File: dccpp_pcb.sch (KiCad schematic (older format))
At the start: 9 parts

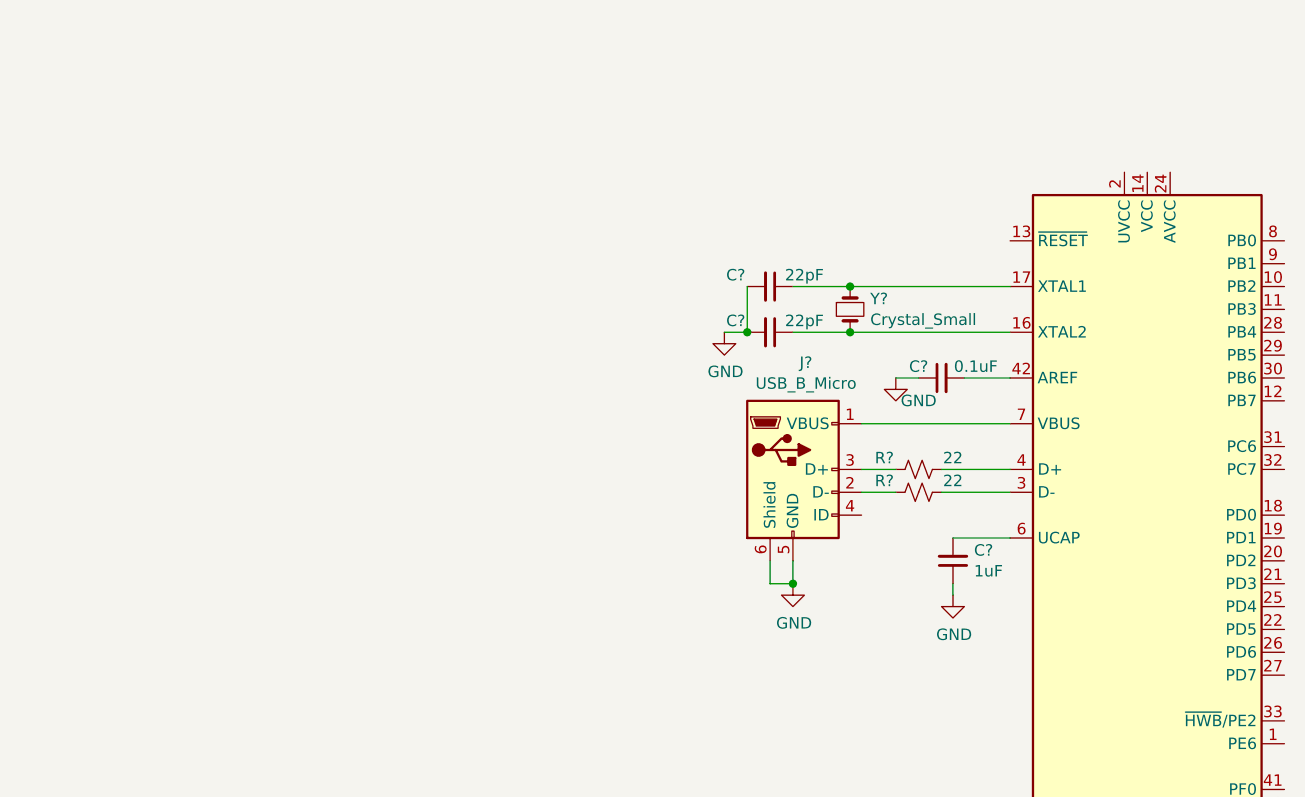
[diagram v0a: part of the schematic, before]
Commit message: Add datasheets and 5V
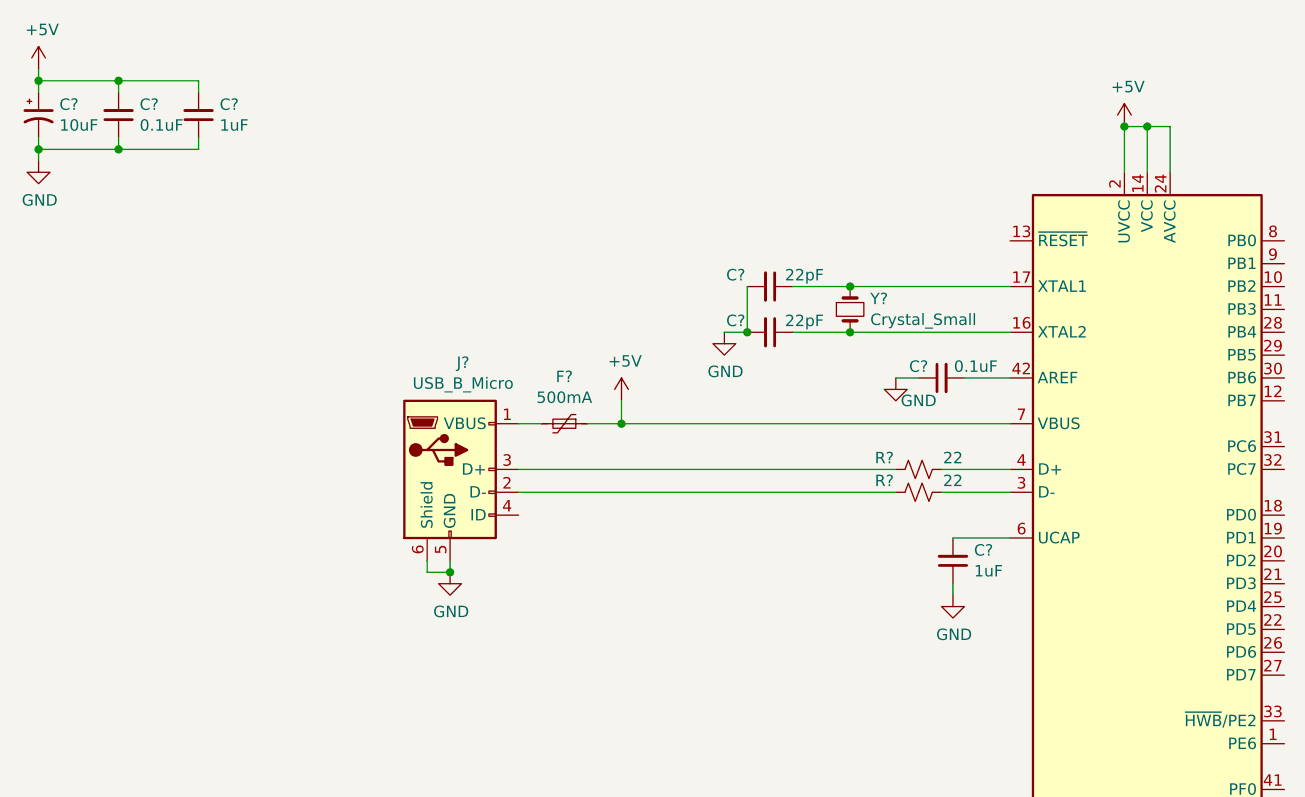
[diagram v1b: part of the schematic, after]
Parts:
- added C?: 1uF, symbol Device:C_Small
- added C?: 0.1uF, symbol Device:C_Small
- added C?: 10uF, symbol Device:CP1_Small
- added F?: 500mA, symbol Device:Polyfuse_Small
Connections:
- net GND: now also C?.1, C?.1, C?.2
- net +5V: now reaches U?.14 (VCC), U?.34 (VCC)
- net +5V: now also U?.2 (UVCC), U?.24 (AVCC), U?.44 (AVCC), U?.7 (VBUS), C?.1, C?.2, C?.2, F?.1
- net at J?.1 (VBUS): now also F?.2; no longer U?.7 (VBUS)
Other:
- moved on the sheet: J?
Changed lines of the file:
@@
 L Connector:USB_B_Micro J?
 U 1 1 5CDAE7D1
-P 4000 2500
-F 0 "J?" H 4057 2967 50  0000 C CNN
-F 1 "USB_B_Micro" H 4057 2876 50  0000 C CNN
-F 2 "" H 4150 2450 50  0001 C CNN
-F 3 "~" H 4150 2450 50  0001 C CNN
-	1    4000 2500
+P 2500 2500
+F 0 "J?" H 2557 2967 50  0000 C CNN
+F 1 "USB_B_Micro" H 2557 2876 50  0000 C CNN
+F 2 "" H 2650 2450 50  0001 C CNN
+F 3 "~" H 2650 2450 50  0001 C CNN
+	1    2500 2500
 	1    0    0    -1
 $EndComp
 Wire Wire Line
 	4450 2100 4550 2100
-Wire Wire Line
-	4300 2300 4950 2300
 $Comp
 L power:GND #PWR?
 U 1 1 5CDB18D1
-P 4000 3000
-F 0 "#PWR?" H 4000 2750 50  0001 C CNN
-F 1 "GND" H 4005 2827 50  0000 C CNN
-F 2 "" H 4000 3000 50  0001 C CNN
-F 3 "" H 4000 3000 50  0001 C CNN
-	1    4000 3000
+P 2500 2950
+F 0 "#PWR?" H 2500 2700 50  0001 C CNN
+F 1 "GND" H 2505 2777 50  0000 C CNN
+F 2 "" H 2500 2950 50  0001 C CNN
+F 3 "" H 2500 2950 50  0001 C CNN
+	1    2500 2950
 	1    0    0    -1
 $EndComp
 Wire Wire Line
-	4000 3000 4000 2900
+	2500 2950 2500 2900
 Wire Wire Line
-	3900 2900 3900 3000
+	2400 2900 2400 2950
 Wire Wire Line
-	3900 3000 4000 3000
-Connection ~ 4000 3000
+	2400 2950 2500 2950
+Connection ~ 2500 2950
 $Comp
 L Device:R_Small_US R?
@@
 $EndComp
 Wire Wire Line
-	4300 2500 4450 2500
+	2800 2500 4450 2500
 Wire Wire Line
-	4450 2600 4300 2600
+	4450 2600 2800 2600
 Wire Wire Line
 	4650 2600 4950 2600
 Wire Wire Line
 	4950 2500 4650 2500
+$Comp
+L Device:Polyfuse_Small F?
+U 1 1 5CDC3346
+P 3000 2300
+F 0 "F?" V 2795 2300 50  0000 C CNN
+F 1 "500mA" V 2886 2300 50  0000 C CNN
+F 2 "" H 3050 2100 50  0001 L CNN
+F 3 "~" H 3000 2300 50  0001 C CNN
+	1    3000 2300
+	0    1    1    0
+$EndComp
+Wire Wire Line
+	2800 2300 2900 2300
+$Comp
+L power:+5V #PWR?
+U 1 1 5CDC41B4
+P 3250 2200
+F 0 "#PWR?" H 3250 2050 50  0001 C CNN
+F 1 "+5V" H 3265 2373 50  0000 C CNN
+F 2 "" H 3250 2200 50  0001 C CNN
+F 3 "" H 3250 2200 50  0001 C CNN
+	1    3250 2200
+	1    0    0    -1
+$EndComp
+$Comp
+L power:+5V #PWR?
+U 1 1 5CDC4BA0
+P 5450 1000
+F 0 "#PWR?" H 5450 850 50  0001 C CNN
+F 1 "+5V" H 5465 1173 50  0000 C CNN
+F 2 "" H 5450 1000 50  0001 C CNN
+F 3 "" H 5450 1000 50  0001 C CNN
+	1    5450 1000
+	1    0    0    -1
+$EndComp
+Wire Wire Line
+	3100 2300 3250 2300
+Wire Wire Line
+	5450 1000 5550 1000
+Wire Wire Line
+	5650 1000 5650 1200
+Wire Wire Line
+	5550 1200 5550 1000
+Connection ~ 5550 1000
+Wire Wire Line
+	5550 1000 5650 1000
+Wire Wire Line
+	5450 1200 5450 1000
+Connection ~ 5450 1000
+$Comp
+L Device:C_Small C?
+U 1 1 5CDC7BF0
+P 1400 950
+F 0 "C?" H 1308 904 50  0000 R CNN
+F 1 "1uF" H 1308 995 50  0000 R CNN
+F 2 "" H 1400 950 50  0001 C CNN
+F 3 "~" H 1400 950 50  0001 C CNN
+	1    1400 950
+	-1   0    0    1
+$EndComp
+$Comp
+L Device:C_Small C?
+U 1 1 5CDCB75C
+P 1050 950
+F 0 "C?" H 958 904 50  0000 R CNN
+F 1 "0.1uF" H 958 995 50  0000 R CNN
+F 2 "" H 1050 950 50  0001 C CNN
+F 3 "~" H 1050 950 50  0001 C CNN
+	1    1050 950
+	-1   0    0    1
+$EndComp
+$Comp
+L Device:CP1_Small C?
+U 1 1 5CDCC558
+P 700 950
+F 0 "C?" H 791 996 50  0000 L CNN
+F 1 "10uF" H 791 905 50  0000 L CNN
+F 2 "" H 700 950 50  0001 C CNN
+F 3 "~" H 700 950 50  0001 C CNN
+	1    700  950
+	1    0    0    -1
+$EndComp
+$Comp
+L power:+5V #PWR?
+U 1 1 5CDE718F
+P 700 750
+F 0 "#PWR?" H 700 600 50  0001 C CNN
+F 1 "+5V" H 715 923 50  0000 C CNN
+F 2 "" H 700 750 50  0001 C CNN
+F 3 "" H 700 750 50  0001 C CNN
+	1    700  750
+	1    0    0    -1
+$EndComp
+Wire Wire Line
+	700  750  700  800
+Wire Wire Line
+	700  800  1050 800
+Wire Wire Line
+	1050 800  1050 850
+Connection ~ 700  800
+Wire Wire Line
+	700  800  700  850
+Wire Wire Line
+	1050 800  1400 800
+Wire Wire Line
+	1400 800  1400 850
+Connection ~ 1050 800
+$Comp
+L power:GND #PWR?
+U 1 1 5CDE9209
+P 700 1150
+F 0 "#PWR?" H 700 900 50  0001 C CNN
+F 1 "GND" H 705 977 50  0000 C CNN
+F 2 "" H 700 1150 50  0001 C CNN
+F 3 "" H 700 1150 50  0001 C CNN
+	1    700  1150
+	1    0    0    -1
+$EndComp
+Wire Wire Line
+	700  1050 700  1100
+Wire Wire Line
+	700  1100 1050 1100
+Wire Wire Line
+	1050 1100 1050 1050
+Connection ~ 700  1100
+Wire Wire Line
+	700  1100 700  1150
+Wire Wire Line
+	1050 1100 1400 1100
+Wire Wire Line
+	1400 1100 1400 1050
+Connection ~ 1050 1100
+Wire Wire Line
+	3250 2300 4950 2300
+Connection ~ 3250 2300
+Wire Wire Line
+	3250 2200 3250 2300
 $EndSCHEMATC

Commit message: Arduino side complete
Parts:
- added R?: 10k, symbol Device:R_Small_US
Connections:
- net +5V: now also R?.2
- net GND: now also U?.15 (GND), U?.23 (GND), U?.35 (GND), U?.43 (GND), U?.5 (UGND)
- net at U?.13 (~RESET): now also R?.1
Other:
- moved on the sheet: C?, F?, J?, R?, U?, Y?

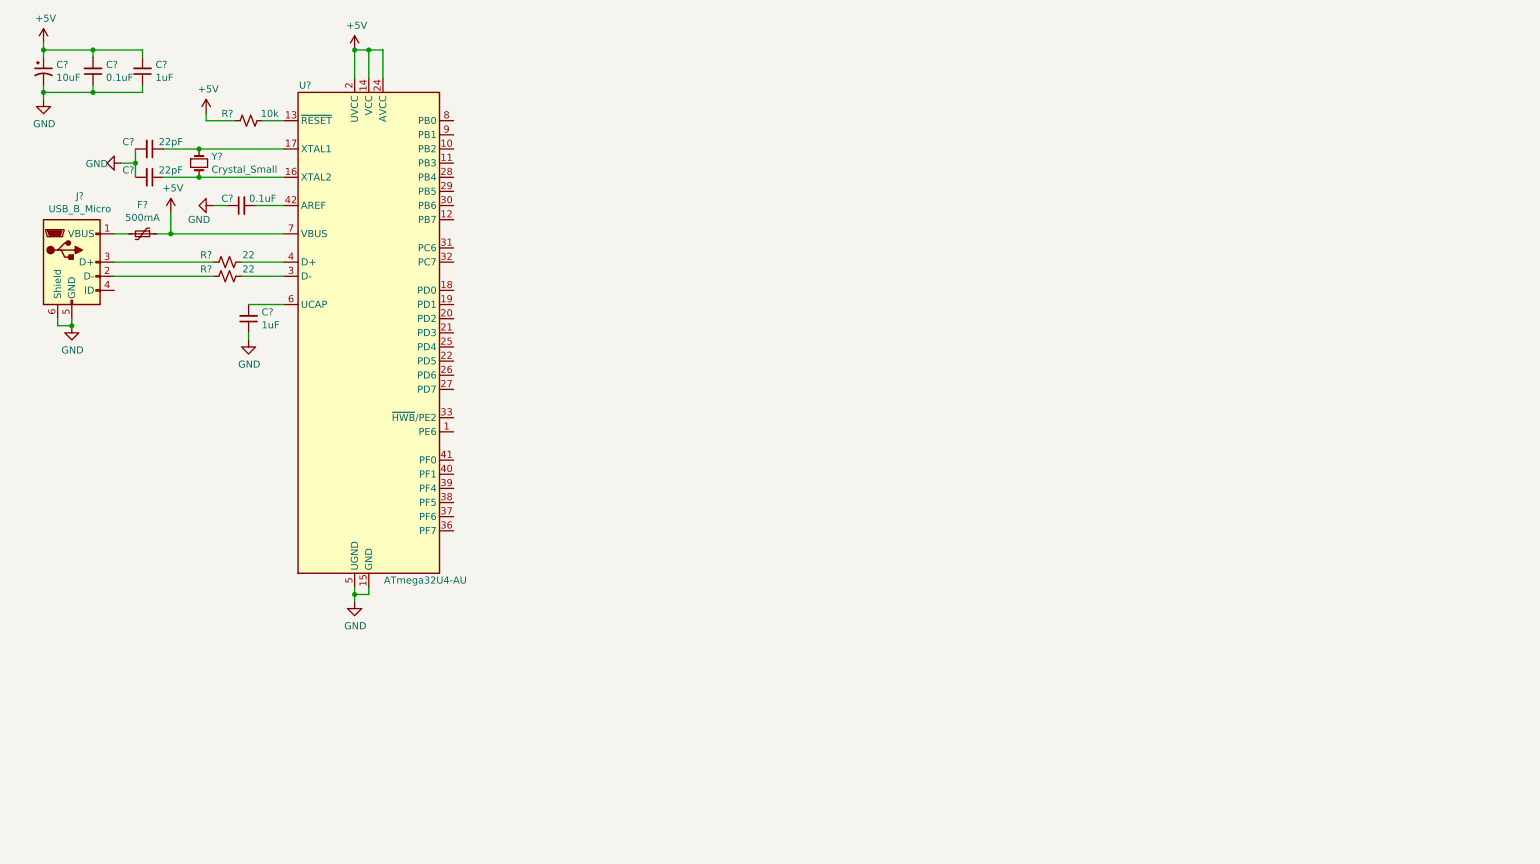
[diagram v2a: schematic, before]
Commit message: Add symbol for IFX007T
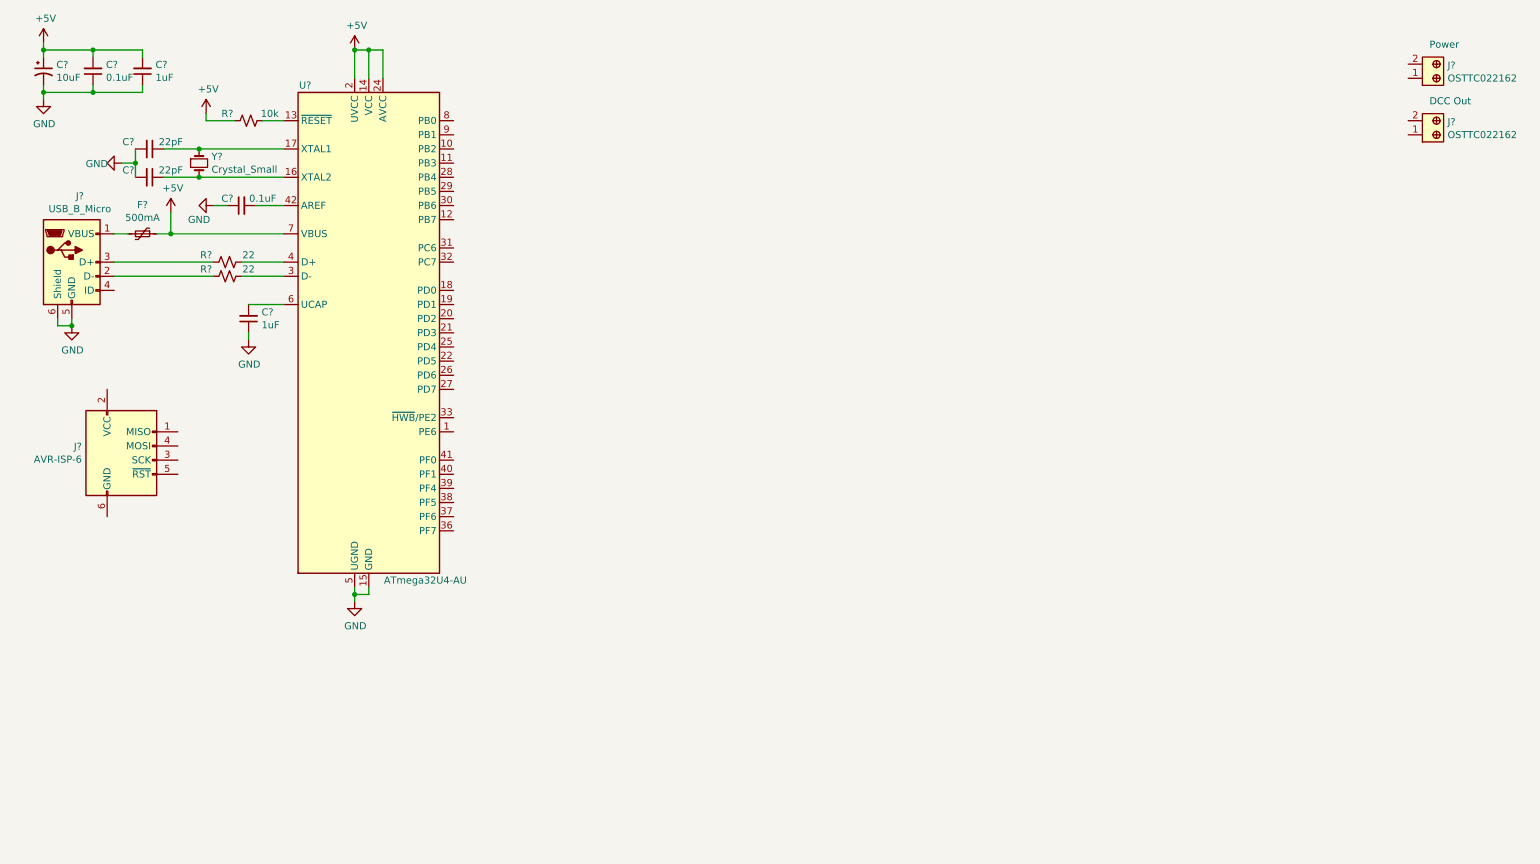
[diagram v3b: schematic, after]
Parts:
- added J?: AVR-ISP-6, symbol Connector:AVR-ISP-6
- added J? (x2): OSTTC022162, digikey-footprints:Term_Block_1x2_P5.08MM, symbol dk_Terminal-Blocks-Wire-to-Board:OSTTC022162
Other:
- note added: "DCC Out"
- note added: "Power"
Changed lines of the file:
@@
 	0    1    1    0
 $EndComp
+$Comp
+L Connector:AVR-ISP-6 J?
+U 1 1 5CE58532
+P 1250 3700
+F 0 "J?" H 971 3796 50  0000 R CNN
+F 1 "AVR-ISP-6" H 971 3705 50  0000 R CNN
+F 2 "" V 1000 3750 50  0001 C CNN
+F 3 " ~" H -25 3150 50  0001 C CNN
+	1    1250 3700
+	1    0    0    -1
+$EndComp
+$Comp
+L dk_Terminal-Blocks-Wire-to-Board:OSTTC022162 J?
+U 1 1 5CE5D8D6
+P 10450 1000
+F 0 "J?" V 10541 822 50  0000 R CNN
+F 1 "OSTTC022162" V 10450 822 50  0000 R CNN
+F 2 "digikey-footprints:Term_Block_1x2_P5.08MM" H 10650 1200 60  0001 L CNN
+F 3 "http://www.on-shore.com/wp-content/uploads/OSTTCXX2162.pdf" H 10650 1300 60  0001 L CNN
+F 4 "ED2609-ND" H 10650 1400 60  0001 L CNN "Digi-Key_PN"
+F 5 "OSTTC022162" H 10650 1500 60  0001 L CNN "MPN"
+F 6 "Connectors, Interconnects" H 10650 1600 60  0001 L CNN "Category"
+F 7 "Terminal Blocks - Wire to Board" H 10650 1700 60  0001 L CNN "Family"
+F 8 "http://www.on-shore.com/wp-content/uploads/OSTTCXX2162.pdf" H 10650 1800 60  0001 L CNN "DK_Datasheet_Link"
+F 9 "/product-detail/en/on-shore-technology-inc/OSTTC022162/ED2609-ND/614558" H 10650 1900 60  0001 L CNN "DK_Detail_Page"
+F 10 "TERM BLK 2P SIDE ENT 5.08MM PCB" H 10650 2000 60  0001 L CNN "Description"
+F 11 "On Shore Technology Inc." H 10650 2100 60  0001 L CNN "Manufacturer"
+F 12 "Active" H 10650 2200 60  0001 L CNN "Status"
+	1    10450 1000
+	0    -1   -1   0
+$EndComp
+$Comp
+L dk_Terminal-Blocks-Wire-to-Board:OSTTC022162 J?
+U 1 1 5CE61EAC
+P 10450 1400
+F 0 "J?" V 10541 1222 50  0000 R CNN
+F 1 "OSTTC022162" V 10450 1222 50  0000 R CNN
+F 2 "digikey-footprints:Term_Block_1x2_P5.08MM" H 10650 1600 60  0001 L CNN
+F 3 "http://www.on-shore.com/wp-content/uploads/OSTTCXX2162.pdf" H 10650 1700 60  0001 L CNN
+F 4 "ED2609-ND" H 10650 1800 60  0001 L CNN "Digi-Key_PN"
+F 5 "OSTTC022162" H 10650 1900 60  0001 L CNN "MPN"
+F 6 "Connectors, Interconnects" H 10650 2000 60  0001 L CNN "Category"
+F 7 "Terminal Blocks - Wire to Board" H 10650 2100 60  0001 L CNN "Family"
+F 8 "http://www.on-shore.com/wp-content/uploads/OSTTCXX2162.pdf" H 10650 2200 60  0001 L CNN "DK_Datasheet_Link"
+F 9 "/product-detail/en/on-shore-technology-inc/OSTTC022162/ED2609-ND/614558" H 10650 2300 60  0001 L CNN "DK_Detail_Page"
+F 10 "TERM BLK 2P SIDE ENT 5.08MM PCB" H 10650 2400 60  0001 L CNN "Description"
+F 11 "On Shore Technology Inc." H 10650 2500 60  0001 L CNN "Manufacturer"
+F 12 "Active" H 10650 2600 60  0001 L CNN "Status"
+	1    10450 1400
+	0    -1   -1   0
+$EndComp
+Text Notes 10500 1200 0    50   ~ 0
+DCC Out
+Text Notes 10500 800  0    50   ~ 0
+Power
 $EndSCHEMATC

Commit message: Add most output circuitry
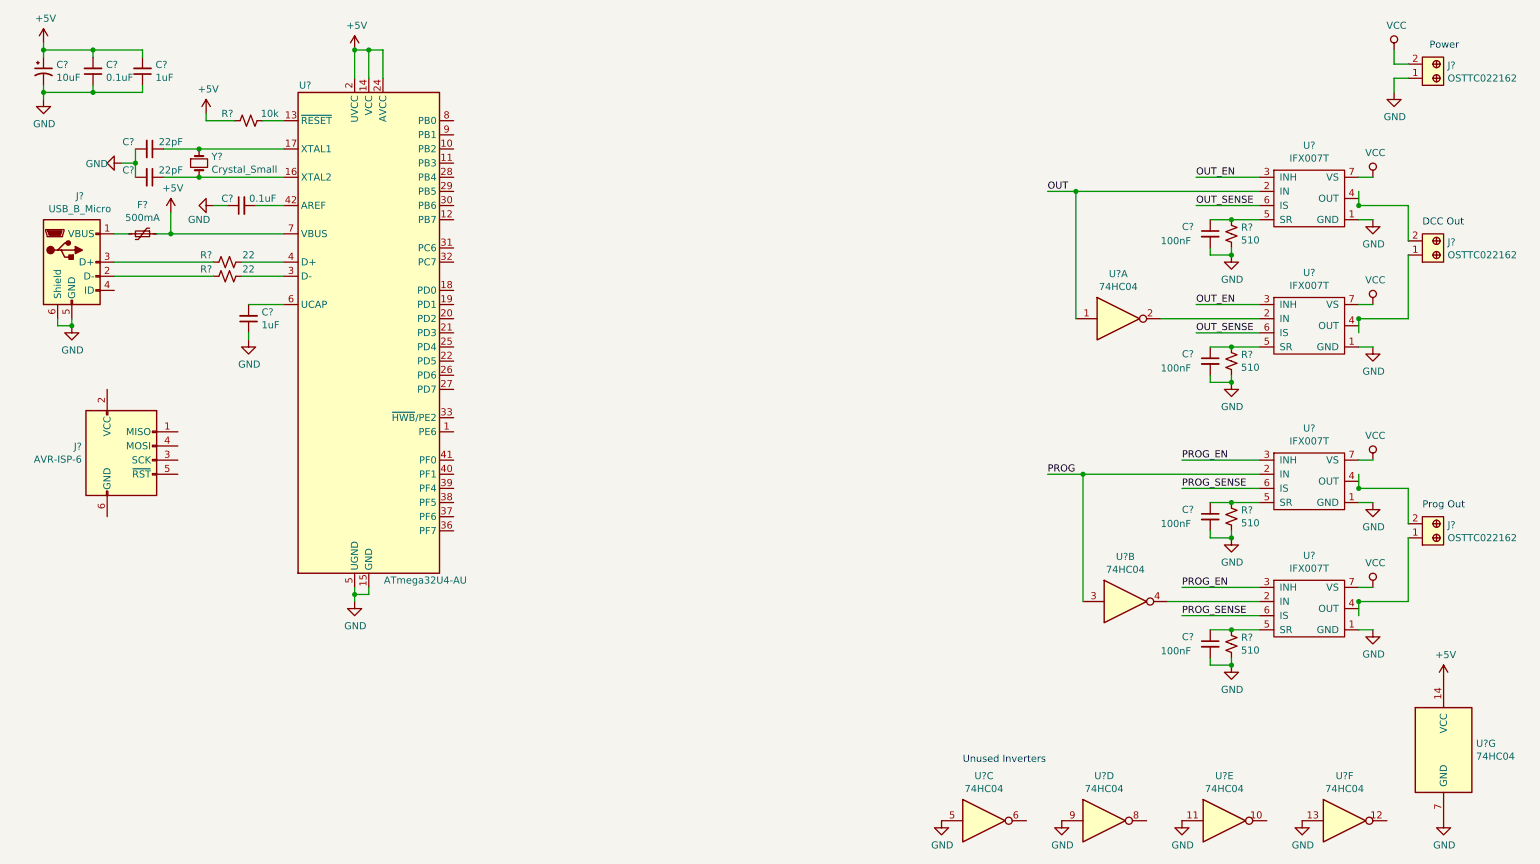
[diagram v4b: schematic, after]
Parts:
- added C? (x4): 100nF, symbol Device:C_Small
- added J?: OSTTC022162, digikey-footprints:Term_Block_1x2_P5.08MM, symbol dk_Terminal-Blocks-Wire-to-Board:OSTTC022162
- added R? (x4): 510, symbol Device:R_Small_US
- added U? (x4): IFX007T, symbol dccpp:IFX007T
- added U? (x7): 74HC04, symbol 74xx:74HC04
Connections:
- net labels added: OUT, OUT_EN, OUT_SENSE, PROG, PROG_EN, PROG_SENSE, VCC
- wire segments 46 -> 106
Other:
- note added: "Prog Out"
- note added: "Unused Inverters"
- moved on the sheet: J?
